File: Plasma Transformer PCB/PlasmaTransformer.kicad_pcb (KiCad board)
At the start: 2 copper layers, 90 x 90 mm, 98 parts, among them J1 Barrel_Jack_MountingPin, J10 Conn_01x01_Socket, J11 Screw_Terminal_01x01, J12 Screw_Terminal_01x01, J13 Conn_01x01_Socket, J14 Conn_01x01_Socket, J15 Conn_01x01_Socket, J16 Conn_01x01_Socket, J17 Conn_01x01_Socket, J18 Conn_01x01_Socket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

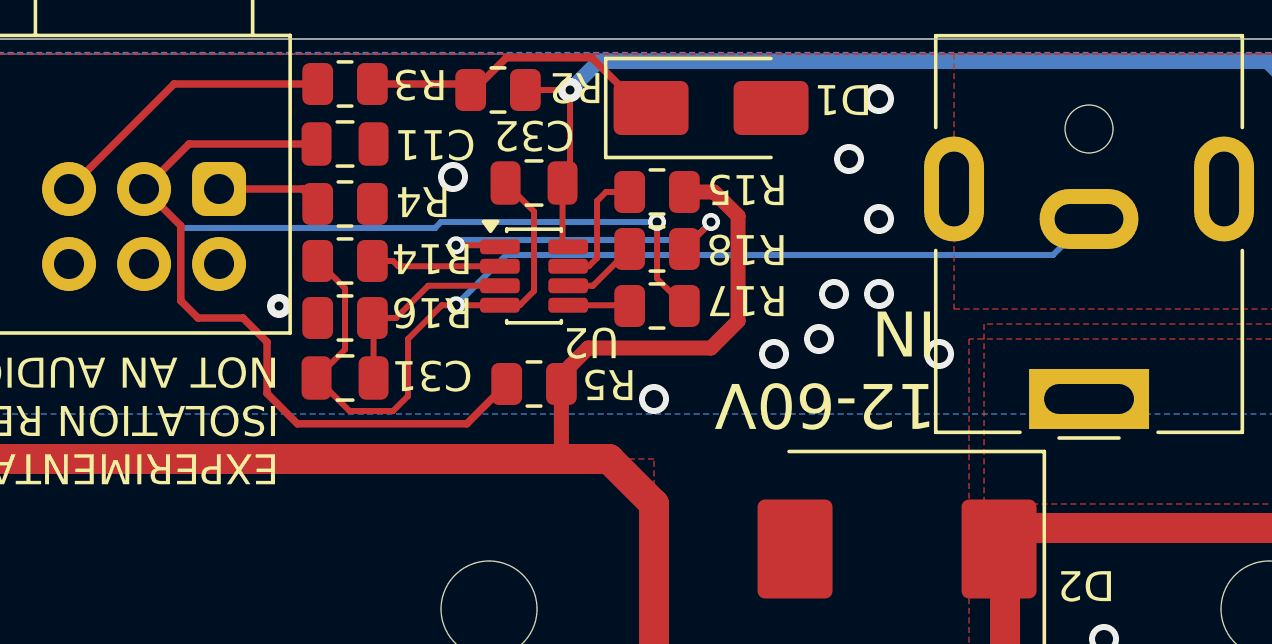
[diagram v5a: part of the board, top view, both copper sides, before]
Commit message: fab fixes, soldermask defined pad for SOT-23-8
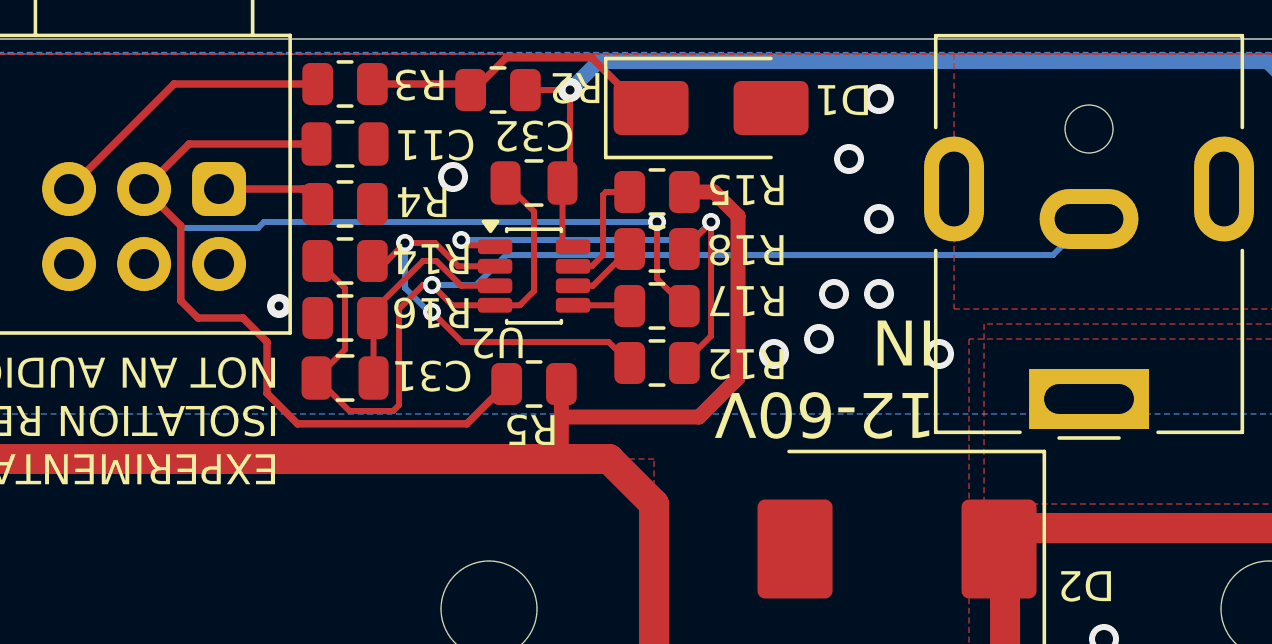
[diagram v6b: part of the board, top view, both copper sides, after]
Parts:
- added R12: 10k, Resistor_SMD:R_0805_2012Metric, F.Cu at (97.6, 65.8)
- U2: footprint Package_TO_SOT_SMD:SOT-23-8 -> ALibrary:SOT-23-8-Soldermask-Defined
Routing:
- net Net-(U2A--): track 4.32 -> 14.8 mm, vias 0 -> 2
- net Net-(R12-Pad2): track 11.6 -> 16.4 mm
- net /GND-IN: track 41.4 -> 43.4 mm
- net /GATE: track 157.4 -> 159.1 mm
- net Net-(U2A-+): track 6.71 -> 7.36 mm
- net GND: vias 30 -> 29
